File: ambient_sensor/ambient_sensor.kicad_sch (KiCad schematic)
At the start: 21 parts, among them J1 Conn_01x02_Pin, J2 Conn_01x02_Pin, J3 Conn_01x05_Pin, J4 Conn_01x01_Pin, J5 Conn_01x04_Pin, J6 Conn_01x02_Pin, U4 ATmega328-P, U6 LD1117S33TR_SOT223, Y1 Crystal

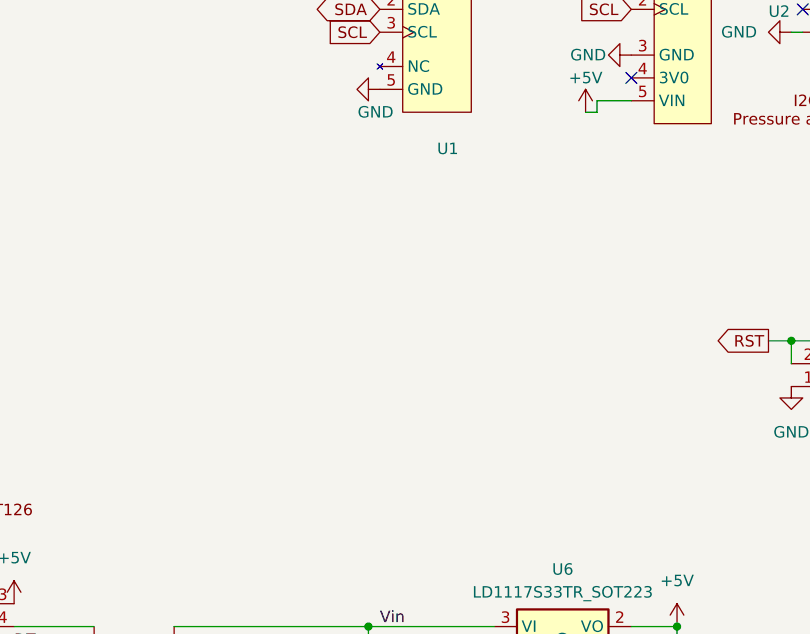
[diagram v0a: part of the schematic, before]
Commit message: USB footprint
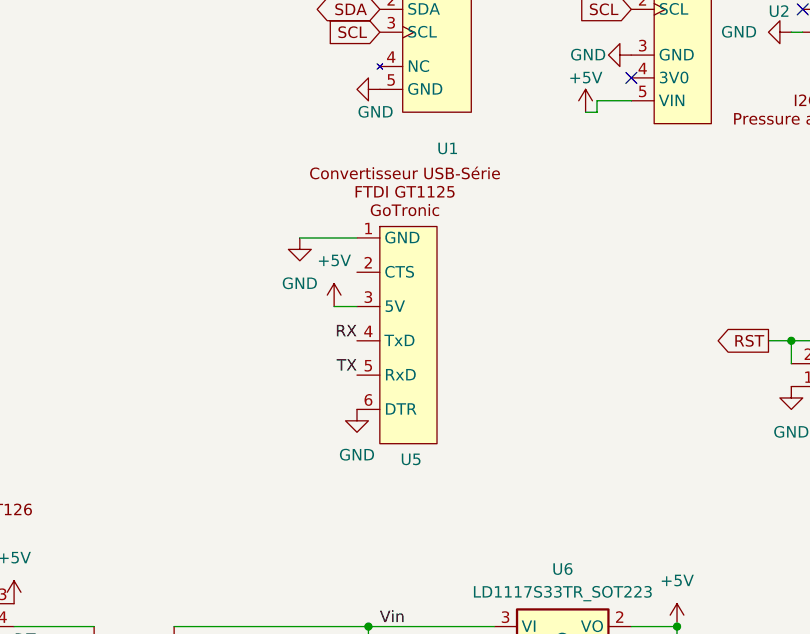
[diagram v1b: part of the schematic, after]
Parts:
- added U5: ~, sensors:USB_FTDI_GT1125, symbol sensors:USB_FTDI_GT1125
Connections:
- net +5V: now also U5.3 (5V)
- net GND: now also U5.1 (GND), U5.6 (DTR)
- net RX: now also U5.4 (TxD)
- net TX: now also U5.5 (RxD)

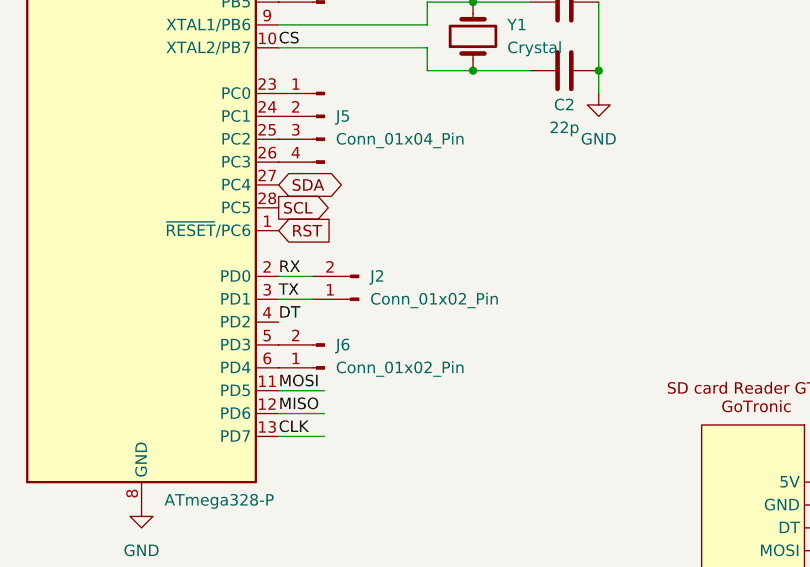
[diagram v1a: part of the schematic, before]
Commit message: USB in the PCB
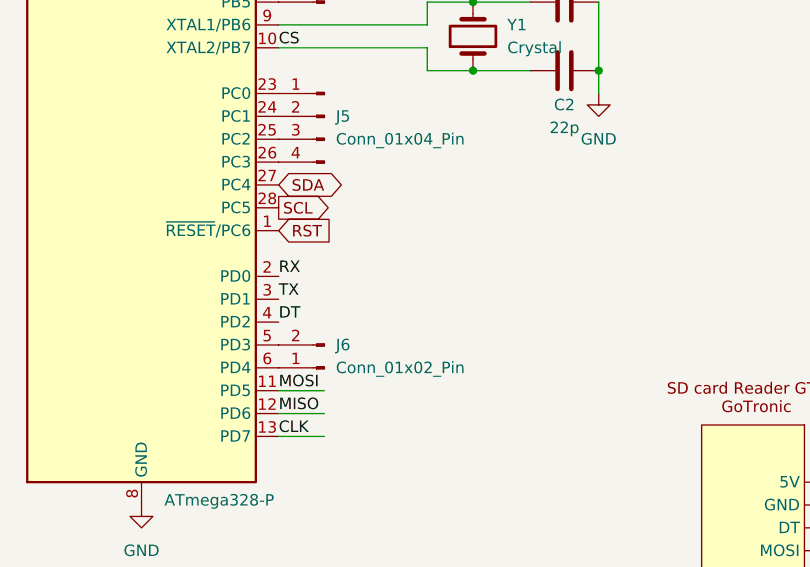
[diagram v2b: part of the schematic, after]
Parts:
- removed J2: Conn_01x02_Pin, Connector_PinHeader_2.54mm:PinHeader_1x02_P2.54mm_Vertical, symbol Connector:Conn_01x02_Pin
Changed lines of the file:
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@@
-	(wire
-		(pts
-			(xy 63.5 72.39) (xy 59.69 72.39)
-		)
-		(stroke
-			(width 0)
-			(type default)
-		)
-	)
 	(wire
 		(pts
@@
 		(pts
 			(xy 76.2 41.91) (xy 76.2 44.45)
-		)
-		(stroke
-			(width 0)
-			(type default)
-		)
-	)
-	(wire
-		(pts
-			(xy 63.5 74.93) (xy 59.69 74.93)
 		)
 		(stroke
@@
 					(unit 1)
 				)
-			)
-		)
-	)
-	(symbol
-		(lib_id "Connector:Conn_01x02_Pin")
-		(at 68.58 74.93 180)
-		(unit 1)
-		(exclude_from_sim no)
-		(in_bom yes)
-		(on_board yes)
-		(dnp no)
-		(fields_autoplaced yes)
-		(property "Reference" "J2"
-			(at 69.85 72.3899 0)
-			(effects
-				(font
-					(size 1.27 1.27)
-				)
-				(justify right)
-			)
-		)
-		(property "Value" "Conn_01x02_Pin"
-			(at 69.85 74.9299 0)
-			(effects
-				(font
-					(size 1.27 1.27)
-				)
-				(justify right)
-			)
-		)
-		(property "Footprint" "Connector_PinHeader_2.54mm:PinHeader_1x02_P2.54mm_Vertical"
-			(at 68.58 74.93 0)
-			(effects
-				(font
-					(size 1.27 1.27)
-				)
-				(hide yes)
-			)
-		)
-		(property "Datasheet" "~"
-			(at 68.58 74.93 0)
-			(effects
-				(font
-					(size 1.27 1.27)
-				)
-				(hide yes)
-			)
-		)
-		(property "Description" "Generic connector, single row, 01x02, script generated"
-			(at 68.58 74.93 0)
-			(effects
-				(font
-					(size 1.27 1.27)
-				)
-				(hide yes)
-			)
-		)
-		(pin "2"
-		)
-		(pin "1"
-		)
-		(instances
-			(project "ambient_sensor"
-				(path "/9e64b25d-56eb-4d28-941d-8d1b0cd0a88c"
-					(reference "J2")
-					(unit 1)
-				)

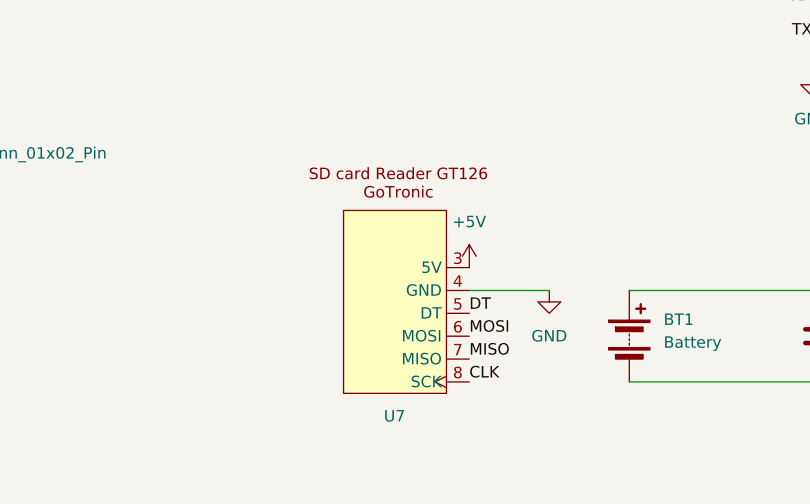
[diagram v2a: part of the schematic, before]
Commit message: fixed sd card reader
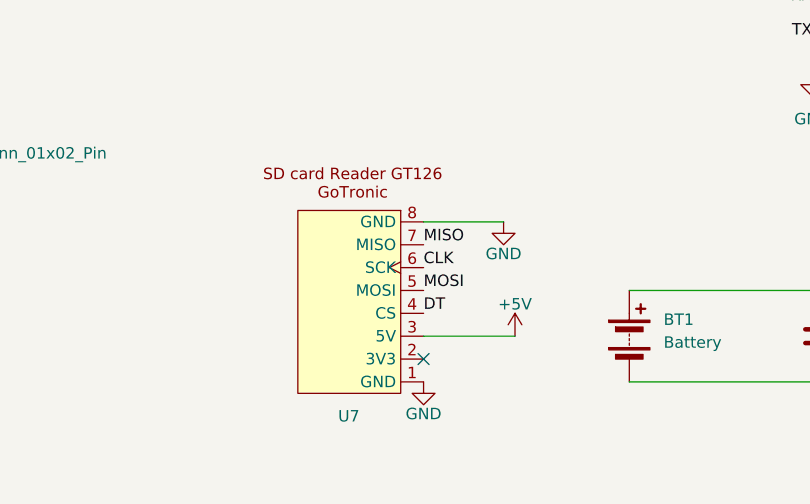
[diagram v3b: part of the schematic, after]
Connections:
- net CLK: now also U7.6 (SCK); no longer U7.8 (SCK)
- net DT: now also U7.4 (CS); no longer U7.5 (DT)
- net GND: now also U7.1 (GND), U7.8 (GND); no longer U7.4 (GND)
- net MOSI: now also U7.5 (MOSI); no longer U7.6 (MOSI)
- no-connect marks 4 -> 5

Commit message: bluetooth module created
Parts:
- added U8: ~, sensors:HC-05_breakboard, symbol sensors:HC-05_breakboard
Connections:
- net +5V: now also U8.5 (VCC)
- net GND: now also U8.4 (GND)
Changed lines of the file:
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@@
+	(wire
+		(pts
+			(xy 116.84 139.7) (xy 119.38 139.7)
+		)
+		(stroke
+			(width 0)
+			(type default)
+		)
+	)
+	(wire
+		(pts
+			(xy 116.84 134.62) (xy 119.38 134.62)
+		)
+		(stroke
+			(width 0)
+			(type default)
+		)
+	)
 	(wire
 		(pts
@@
 	)
 	(symbol
+		(lib_id "power:+5V")
+		(at 119.38 134.62 0)
+		(unit 1)
+		(exclude_from_sim no)
+		(in_bom yes)
+		(on_board yes)
+		(dnp no)
+		(property "Reference" "#PWR023"
+			(at 119.38 138.43 0)
+			(effects
+				(font
+					(size 1.27 1.27)
+				)
+				(hide yes)
+			)
+		)
+		(property "Value" "+5V"
+			(at 119.38 131.064 0)
+			(effects
+				(font
+					(size 1.27 1.27)
+				)
+			)
+		)
+		(property "Footprint" ""
+			(at 119.38 134.62 0)
+			(effects
+				(font
+					(size 1.27 1.27)
+				)
+				(hide yes)
+			)
+		)
+		(property "Datasheet" ""
+			(at 119.38 134.62 0)
+			(effects
+				(font
+					(size 1.27 1.27)
+				)
+				(hide yes)
+			)
+		)
+		(property "Description" "Power symbol creates a global label with name \"+5V\""
+			(at 119.38 134.62 0)
+			(effects
+				(font
+					(size 1.27 1.27)
+				)
+				(hide yes)
+			)
+		)
+		(pin "1"
+		)
+		(instances
+			(project "ambient_sensor"
+				(path "/9e64b25d-56eb-4d28-941d-8d1b0cd0a88c"
+					(reference "#PWR023")
+					(unit 1)
+				)
+			)
+		)
+	)
+	(symbol
 		(lib_id "power:GND")
 		(at 44.45 97.79 0)
@@
 	)
 	(symbol
+		(lib_id "sensors:HC-05_breakboard")
+		(at 107.95 146.05 0)
+		(unit 1)
+		(exclude_from_sim no)
+		(in_bom yes)
+		(on_board yes)
+		(dnp no)
+		(fields_autoplaced yes)
+		(property "Reference" "U8"
+			(at 107.95 115.57 0)
+			(effects
+				(font
+					(size 1.27 1.27)
+				)
+			)
+		)
+		(property "Value" "~"
+			(at 107.95 116.84 0)
+			(effects
+				(font
+					(size 1.27 1.27)
+				)
+			)
+		)
+		(property "Footprint" "sensors:HC-05_breakboard"
+			(at 107.95 146.05 0)
+			(effects
+				(font
+					(size 1.27 1.27)
+				)
+				(hide yes)
+			)
+		)
+		(property "Datasheet" ""
+			(at 107.95 146.05 0)
+			(effects
+				(font
+					(size 1.27 1.27)
+				)
+				(hide yes)
+			)
+		)
+		(property "Description" ""
+			(at 107.95 146.05 0)
+			(effects
+				(font
+					(size 1.27 1.27)
+				)
+				(hide yes)
+			)
+		)
+		(pin "1"
+		)
+		(pin "2"
+		)
+		(pin "5"
+		)
+		(pin "4"
+		)
+		(pin "3"
+		)
+		(pin "6"
+		)
+		(instances
+			(project ""
+				(path "/9e64b25d-56eb-4d28-941d-8d1b0cd0a88c"
+					(reference "U8")
+					(unit 1)
+				)
+			)
+		)
+	)
+	(symbol
 		(lib_id "power:GND")
 		(at 189.23 34.29 270)
@@
 					(unit 1)
 				)
+			)
+		)
+	)
+	(symbol
+		(lib_id "power:GND")
+		(at 119.38 139.7 0)
+		(mirror y)
+		(unit 1)
+		(exclude_from_sim no)
+		(in_bom yes)
+		(on_board yes)
+		(dnp no)
+		(property "Reference" "#PWR024"
+			(at 119.38 146.05 0)
+			(effects
+				(font
+					(size 1.27 1.27)
+				)
+				(hide yes)
+			)
+		)
+		(property "Value" "GND"
+			(at 119.38 143.256 0)
+			(effects
+				(font
+					(size 1.27 1.27)
+				)
+			)
+		)
+		(property "Footprint" ""
+			(at 119.38 139.7 0)
+			(effects
+				(font
+					(size 1.27 1.27)
+				)
+				(hide yes)
+			)
+		)
+		(property "Datasheet" ""
+			(at 119.38 139.7 0)
+			(effects
+				(font
+					(size 1.27 1.27)
+				)
+				(hide yes)
+			)
+		)
+		(property "Description" "Power symbol creates a global label with name \"GND\" , ground"
+			(at 119.38 139.7 0)
+			(effects
+				(font
+					(size 1.27 1.27)
+				)
+				(hide yes)
+			)
+		)
+		(pin "1"
+		)
+		(instances
+			(project "ambient_sensor"
+				(path "/9e64b25d-56eb-4d28-941d-8d1b0cd0a88c"
+					(reference "#PWR024")
+					(unit 1)
+				)

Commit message: rudimentary bluetooth
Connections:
- net CLK: now also J3.5 (Pin_5), U4.19 (PB5); no longer U4.13 (PD7)
- net RxS: now reaches J3.1 (Pin_1), U4.15 (PB1)
- net RxS: now also U8.3 (TxD)
- net TxS: now reaches J3.2 (Pin_2), U4.16 (PB2)
- net TxS: now also U8.2 (RxD)
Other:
- moved on the sheet: J3
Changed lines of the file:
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@@
+	(wire
+		(pts
+			(xy 62.23 31.75) (xy 59.69 31.75)
+		)
+		(stroke
+			(width 0)
+			(type default)
+		)
+	)
 	(wire
 		(pts
@@
 	(wire
 		(pts
+			(xy 62.23 36.83) (xy 59.69 36.83)
+		)
+		(stroke
+			(width 0)
+			(type default)
+		)
+	)
+	(wire
+		(pts
 			(xy 116.84 139.7) (xy 119.38 139.7)
 		)
@@
 	(wire
 		(pts
-			(xy 59.69 90.17) (xy 64.77 90.17)
-		)
-		(stroke
-			(width 0)
-			(type default)
-		)
-	)
-	(wire
-		(pts
 			(xy 59.69 46.99) (xy 76.2 46.99)
 		)
@@
 	(wire
 		(pts
+			(xy 62.23 41.91) (xy 59.69 41.91)
+		)
+		(stroke
+			(width 0)
+			(type default)
+		)
+	)
+	(wire
+		(pts
 			(xy 194.31 107.95) (xy 181.61 107.95)
 		)
@@
 	(wire
 		(pts
+			(xy 62.23 34.29) (xy 59.69 34.29)
+		)
+		(stroke
+			(width 0)
+			(type default)
+		)
+	)
+	(wire
+		(pts
+			(xy 62.23 39.37) (xy 59.69 39.37)
+		)
+		(stroke
+			(width 0)
+			(type default)
+		)
+	)
+	(wire
+		(pts
 			(xy 76.2 41.91) (xy 76.2 44.45)
 		)
@@
 			(width 0)
 			(type default)
+		)
+	)
+	(label "RxS"
+		(at 99.06 139.7 180)
+		(fields_autoplaced yes)
+		(effects
+			(font
+				(size 1.27 1.27)
+			)
+			(justify right bottom)
+		)
+	)
+	(label "TxS"
+		(at 99.06 135.89 180)
+		(fields_autoplaced yes)
+		(effects
+			(font
+				(size 1.27 1.27)
+			)
+			(justify right bottom)
 		)
 	)
@@
 		)
 	)
+	(label "CLK"
+		(at 59.69 41.91 0)
+		(fields_autoplaced yes)
+		(effects
+			(font
+				(size 1.27 1.27)
+			)
+			(justify left bottom)
+		)
+	)
 	(label "TX"
 		(at 158.75 69.85 180)
@@
 		)
 	)
+	(label "RxS"
+		(at 59.69 31.75 0)
+		(fields_autoplaced yes)
+		(effects
+			(font
+				(size 1.27 1.27)
+			)
+			(justify left bottom)
+		)
+	)
+	(label "TxS"
+		(at 59.69 34.29 0)
+		(fields_autoplaced yes)
+		(effects
+			(font
+				(size 1.27 1.27)
+			)
+			(justify left bottom)
+		)
+	)
 	(label "MISO"
 		(at 59.69 87.63 0)
@@
 	(label "TX"
 		(at 59.69 74.93 0)
-		(fields_autoplaced yes)
-		(effects
-			(font
-				(size 1.27 1.27)
-			)
-			(justify left bottom)
-		)
-	)
-	(label "CLK"
-		(at 59.69 90.17 0)
 		(fields_autoplaced yes)
 		(effects
@@
 	(symbol
 		(lib_id "Connector:Conn_01x05_Pin")
-		(at 64.77 36.83 0)
+		(at 67.31 36.83 0)
 		(mirror y)
 		(unit 1)
@@
 		(fields_autoplaced yes)
 		(property "Reference" "J3"
-			(at 66.04 35.5599 0)
+			(at 68.58 35.5599 0)
 			(effects
 				(font
@@
 		)
 		(property "Value" "Conn_01x05_Pin"
-			(at 66.04 38.0999 0)
+			(at 68.58 38.0999 0)
 			(effects
 				(font
@@
 		)
 		(property "Footprint" "Connector_PinHeader_2.54mm:PinHeader_1x05_P2.54mm_Vertical"
-			(at 64.77 36.83 0)
+			(at 67.31 36.83 0)
 			(effects
 				(font
@@
 		)
 		(property "Datasheet" "~"
-			(at 64.77 36.83 0)
+			(at 67.31 36.83 0)
 			(effects
 				(font
@@
 		)
 		(property "Description" "Generic connector, single row, 01x05, script generated"
-			(at 64.77 36.83 0)
-			(effects
-				(font
+			(at 67.31 36.83 0)
+			(effects
+				(font

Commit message: before impleenting the changes
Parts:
- added D2: LED, LED_SMD:LED_1206_3216Metric, symbol Device:LED
- added R3: 1k, Resistor_SMD:R_1206_3216Metric, symbol Device:R
- R1: value 120 -> 1k
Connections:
- net GND: now also D2.1 (K)
- net TxS: now also J4.1 (Pin_1), U4.14 (PB0); no longer J3.2 (Pin_2), U4.16 (PB2)
- net LED_BUILTIN: now reaches J5.1 (Pin_1), U4.23 (PC0)
- net LED_BUILTIN: now also R3.1
- new net: J3.2 (Pin_2), U4.16 (PB2)
- new net: D2.2 (A), R3.2
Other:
- moved on the sheet: J4, J5
